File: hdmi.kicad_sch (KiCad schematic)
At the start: 43 parts, among them J13 46756-1001, Q22 NX138BKMYL, U43 NTS0102GT, U44 TPD4E02B04DQA, U45 TPD4E02B04DQA, U46 TPD4E02B04DQA

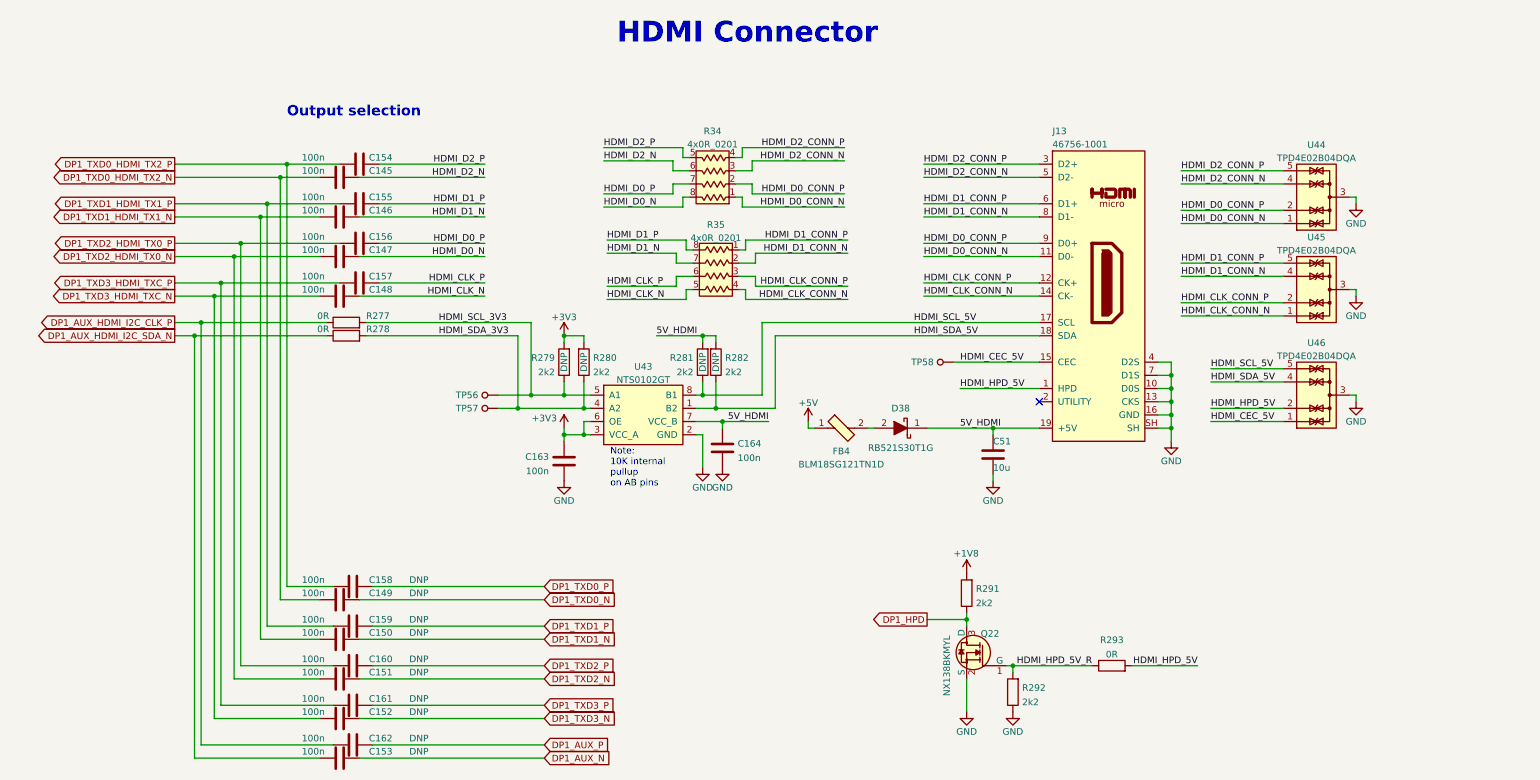
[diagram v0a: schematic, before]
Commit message: Routed high speed HDMI/DP
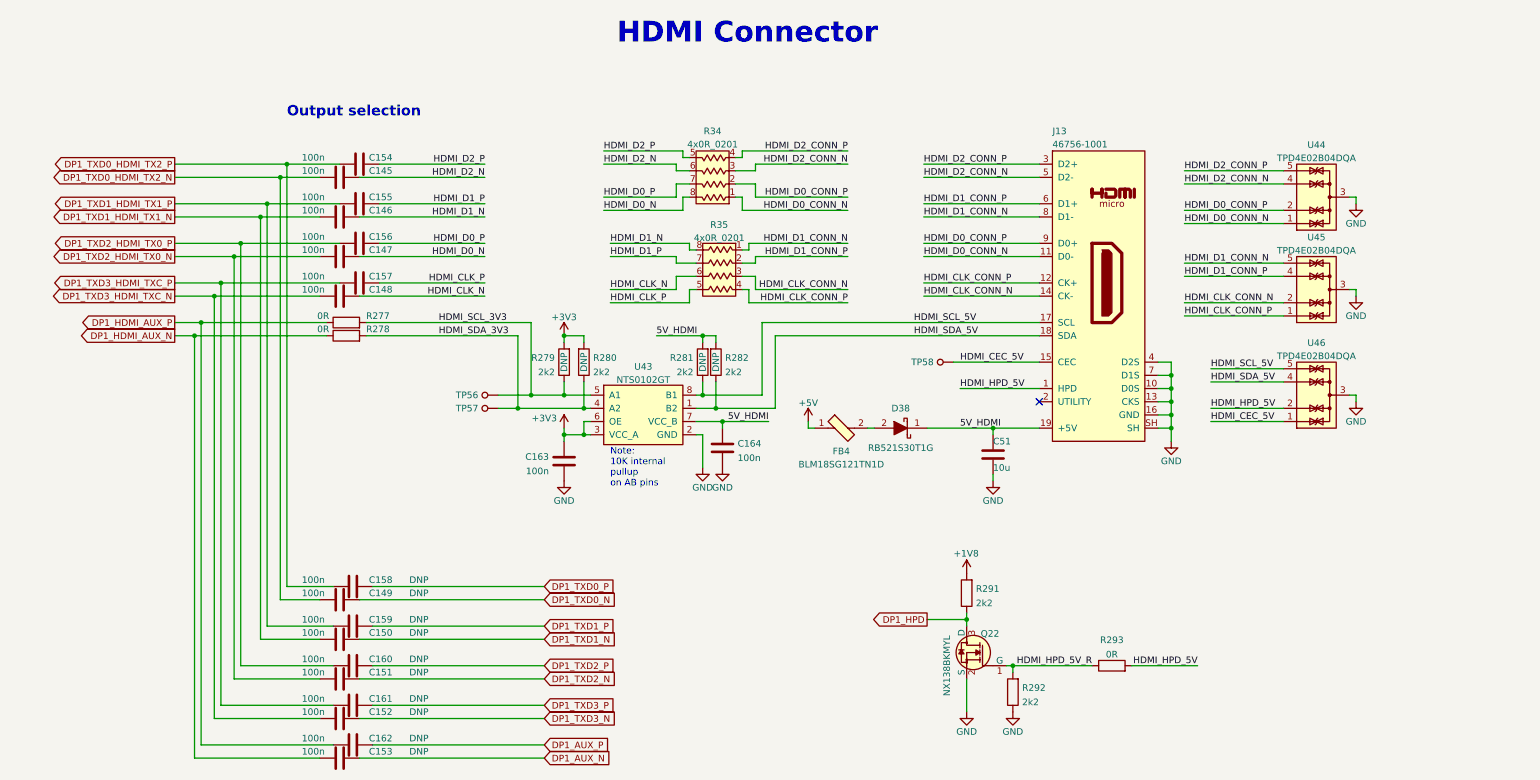
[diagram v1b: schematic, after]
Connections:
- net HDMI_CLK_CONN_N: now also R35.3, U45.2 (IO2), U45.9 (NC); no longer R35.4, U45.1 (IO1), U45.10 (NC)
- net HDMI_CLK_CONN_P: now also R35.4, U45.1 (IO1), U45.10 (NC); no longer R35.3, U45.2 (IO2), U45.9 (NC)
- net HDMI_CLK_N: now also R35.6; no longer R35.5
- net HDMI_CLK_P: now also R35.5; no longer R35.6
- net HDMI_D1_CONN_N: now also R35.1, U45.5 (IO4), U45.6 (NC); no longer R35.2, U45.4 (IO3), U45.7 (NC)
- net HDMI_D1_CONN_P: now also R35.2, U45.4 (IO3), U45.7 (NC); no longer R35.1, U45.5 (IO4), U45.6 (NC)
- net HDMI_D1_N: now also R35.8; no longer R35.7
- net HDMI_D1_P: now also R35.7; no longer R35.8
- net DP1_AUX_HDMI_I2C_CLK_P renamed DP1_HDMI_AUX_P
- net DP1_AUX_HDMI_I2C_SDA_N renamed DP1_HDMI_AUX_N
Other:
- moved on the sheet: R35

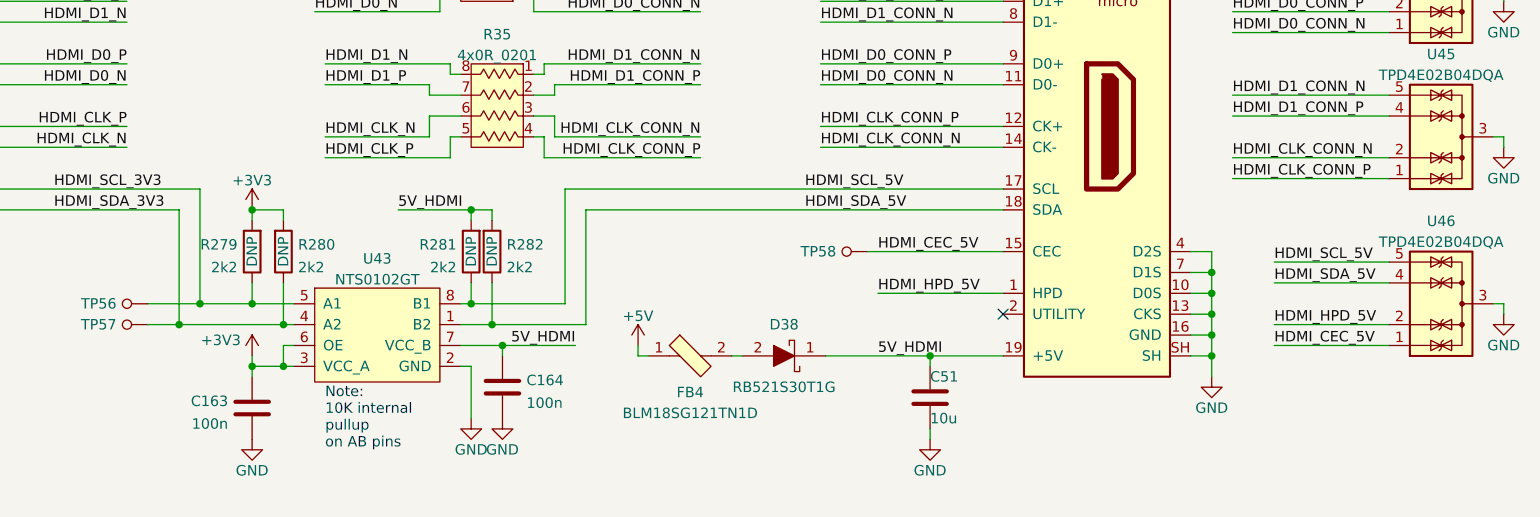
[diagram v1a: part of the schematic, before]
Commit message: Routed more low speed signal and power
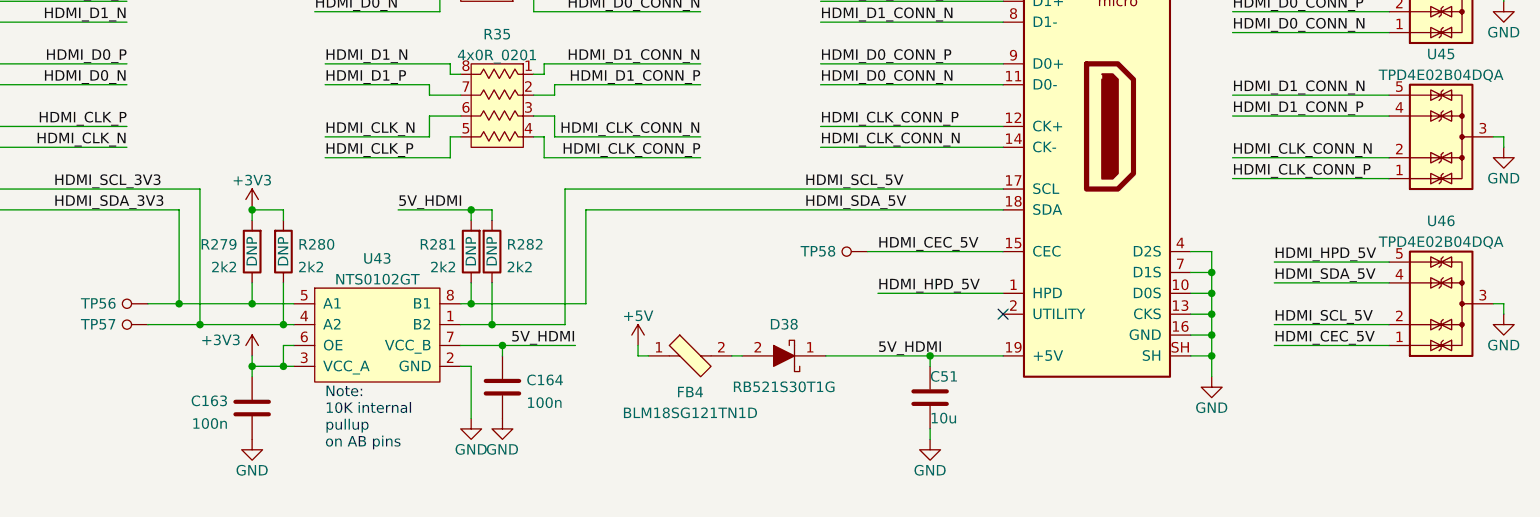
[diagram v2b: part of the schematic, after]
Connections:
- net HDMI_HPD_5V: now also U46.5 (IO4), U46.6 (NC); no longer U46.2 (IO2), U46.9 (NC)
- net HDMI_SCL_3V3: now also R280.1, TP57.1, U43.4 (A2); no longer R279.1, TP56.1, U43.5 (A1)
- net HDMI_SCL_5V: now also R282.1, U43.1 (B2), U46.2 (IO2), U46.9 (NC); no longer R281.1, U43.8 (B1), U46.5 (IO4), U46.6 (NC)
- net HDMI_SDA_3V3: now also R279.1, TP56.1, U43.5 (A1); no longer R280.1, TP57.1, U43.4 (A2)
- net HDMI_SDA_5V: now also R281.1, U43.8 (B1); no longer R282.1, U43.1 (B2)

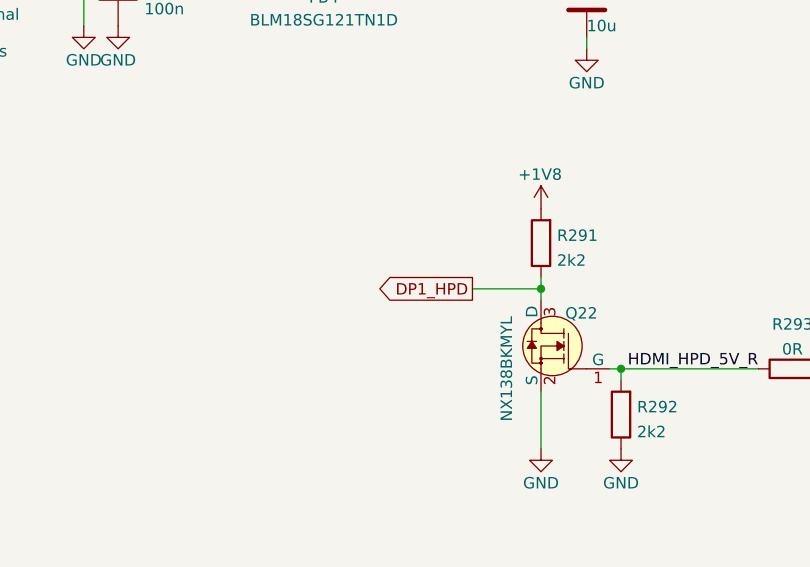
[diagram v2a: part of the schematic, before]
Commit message: CSchematic changes after review
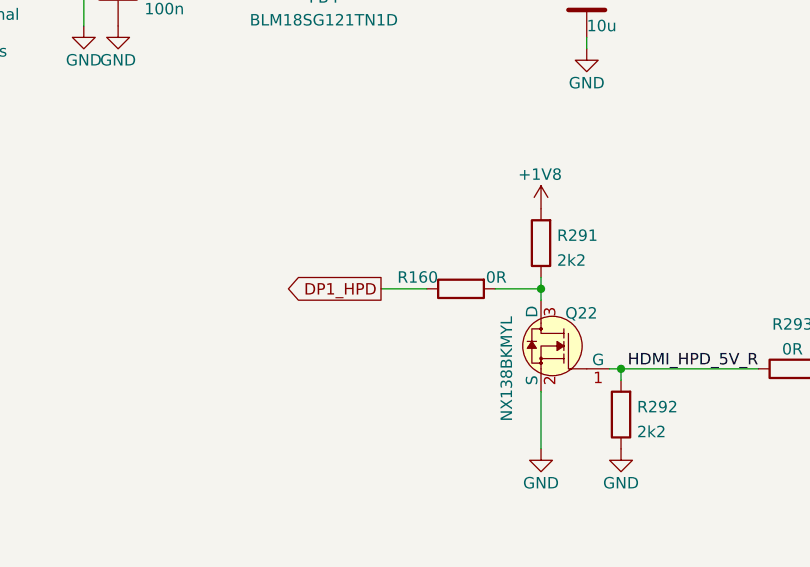
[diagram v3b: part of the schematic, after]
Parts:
- added R160: R_0R_0402, antmicro-footprints:0402-res, symbol antmicroResistors0402:R_0R_0402
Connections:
- net DP1_HPD: now also R160.1; no longer Q22.3 (D), R291.1
- new net: Q22.3 (D), R160.2, R291.1
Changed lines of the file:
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@@
   (junction (at 109.22 106.68) (diameter 0) (color 0 0 0 0)
   )
-  (junction (at 250.19 176.53) (diameter 0) (color 0 0 0 0)
-  )
   (junction (at 110.49 104.14) (diameter 0) (color 0 0 0 0)
   )
+  (junction (at 250.19 176.53) (diameter 0) (color 0 0 0 0)
+  )
   (junction (at 101.6 121.92) (diameter 0) (color 0 0 0 0)
   )
@@
     (stroke (width 0) (type default) (color 0 0 0 0))
   )
-  (wire (pts (xy 242.57 176.53) (xy 250.19 176.53))
-    (stroke (width 0) (type default) (color 0 0 0 0))
-  )
   (wire (pts (xy 247.65 127) (xy 264.16 127))
     (stroke (width 0) (type default) (color 0 0 0 0))
@@
     (stroke (width 0) (type default) (color 0 0 0 0))
   )
+  (wire (pts (xy 245.11 176.53) (xy 250.19 176.53))
+    (stroke (width 0) (type default) (color 0 0 0 0))
+  )
   (wire (pts (xy 168.91 170.18) (xy 135.89 170.18))
     (stroke (width 0) (type default) (color 0 0 0 0))
@@
     (stroke (width 0) (type default) (color 0 0 0 0))
   )
+  (wire (pts (xy 250.19 176.53) (xy 250.19 177.8))
+    (stroke (width 0) (type default) (color 0 0 0 0))
+  )
   (wire (pts (xy 166.37 135.89) (xy 176.53 135.89))
     (stroke (width 0) (type default) (color 0 0 0 0))
@@
     (stroke (width 0) (type default) (color 0 0 0 0))
   )
-  (wire (pts (xy 250.19 177.8) (xy 250.19 176.53))
+  (wire (pts (xy 250.19 175.26) (xy 250.19 176.53))
     (stroke (width 0) (type default) (color 0 0 0 0))
   )
@@
     (stroke (width 0) (type default) (color 0 0 0 0))
   )
-  (wire (pts (xy 250.19 175.26) (xy 250.19 176.53))
-    (stroke (width 0) (type default) (color 0 0 0 0))
-  )
   (wire (pts (xy 106.68 193.04) (xy 128.27 193.04))
     (stroke (width 0) (type default) (color 0 0 0 0))
@@
     (stroke (width 0) (type default) (color 0 0 0 0))
   )
+  (wire (pts (xy 232.41 176.53) (xy 237.49 176.53))
+    (stroke (width 0) (type default) (color 0 0 0 0))
+  )
   (wire (pts (xy 177.8 138.43) (xy 176.53 138.43))
     (stroke (width 0) (type default) (color 0 0 0 0))
@@
     )
   )
-  (global_label "DP1_HPD" (shape output) (at 242.57 176.53 180)
+  (global_label "DP1_HPD" (shape output) (at 232.41 176.53 180)
     (effects (font (size 1.27 1.27)) (justify right))
-    (property "Intersheet References" "${INTERSHEET_REFS}" (id 0) (at 228.6 176.53 0)
+    (property "Intersheet References" "${INTERSHEET_REFS}" (id 0) (at 218.44 176.53 0)
       (effects (font (size 1.27 1.27)) (justify right))
     )
@@
     (pin "1")
     (pin "2")
+  )
+  (symbol (lib_id "antmicroResistors0402:R_0R_0402") (at 241.3 176.53 0) (mirror x) (unit 1)
+    (in_bom yes) (on_board yes)
+    (property "Reference" "R160" (id 0) (at 238.76 175.26 0)
+      (effects (font (size 1.27 1.27)) (justify right))
+    )
+    (property "Value" "R_0R_0402" (id 1) (at 241.3 172.72 0)
+      (effects (font (size 1.27 1.27)) hide)
+    )
+    (property "Footprint" "antmicro-footprints:0402-res" (id 2) (at 246.38 181.61 0)
+      (effects (font (size 1.524 1.524)) (justify left) hide)
+    )
+    (property "Datasheet" "" (id 3) (at 241.3 176.53 0)
+      (effects (font (size 1.27 1.27)) hide)
+    )
+    (property "Manufacturer" "PANASONIC" (id 4) (at 246.38 186.69 0)
+      (effects (font (size 1.524 1.524)) (justify left) hide)
+    )
+    (property "MPN" "ERJ2GE0R00X" (id 5) (at 246.38 184.15 0)
+      (effects (font (size 1.524 1.524)) (justify left) hide)
+    )
+    (property "Val" "0R" (id 6) (at 246.38 175.26 0)
+      (effects (font (size 1.27 1.27)) (justify right))
+    )
+    (pin "1")
+    (pin "2")

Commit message: Loclib
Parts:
- C145, C146, C147, C148, C149, C150, C151, C152, C153, C154, C155, C156, C157, C158, C159, C160, C161, C162, C163, C164: footprint antmicro-footprints:0402-cap -> jetson-orin-baseboard-footprints:0402-cap; symbol antmicroCapacitors0402:C_100n_0402 -> jetson-orin-baseboard:C_100n_0402
- C51: footprint antmicro-footprints:0603-cap -> jetson-orin-baseboard-footprints:0603-cap; symbol antmicroCapacitors0603:C_10u_0603 -> jetson-orin-baseboard:C_10u_0603
- D38: footprint antmicro-footprints:SOD-523 -> jetson-orin-baseboard-footprints:SOD-523; symbol antmicroDiodesRectifiersSingle:RB521S30T1G -> jetson-orin-baseboard:RB521S30T1G
- FB4: footprint antmicro-footprints:0603-res -> jetson-orin-baseboard-footprints:0603-res; symbol antmicroFerriteBeadsandChips:BLM18SG121TN1D -> jetson-orin-baseboard:BLM18SG121TN1D
- J13: footprint antmicro-footprints:HDMI_Micro-D_Molex_46765-1x01 -> jetson-orin-baseboard-footprints:HDMI_Micro-D_Molex_46765-1x01; symbol antmicroUSBDVIHDMIConnectors:46756-1001 -> jetson-orin-baseboard:46756-1001
- Q22: footprint antmicro-footprints:DFN1006-3 -> jetson-orin-baseboard-footprints:DFN1006-3; symbol antmicroTransistorsFETsMOSFETsSingle:NX138BKMYL -> jetson-orin-baseboard:NX138BKMYL
- R160, R277, R278, R293: footprint antmicro-footprints:0402-res -> jetson-orin-baseboard-footprints:0402-res; symbol antmicroResistors0402:R_0R_0402 -> jetson-orin-baseboard:R_0R_0402
- R279, R280, R281, R282, R291, R292: footprint antmicro-footprints:0402-res -> jetson-orin-baseboard-footprints:0402-res; symbol antmicroResistors0402:R_2k2_0402 -> jetson-orin-baseboard:R_2k2_0402
- R34, R35: footprint antmicro-footprints:EXB18V -> jetson-orin-baseboard-footprints:EXB18V; symbol antmicroResistorNetworksArrays:4x0R_0201_array -> jetson-orin-baseboard:4x0R_0201_array
- TP56, TP57, TP58: footprint antmicro-footprints:Testpoint_smd_0_75mm -> jetson-orin-baseboard-footprints:Testpoint_smd_0_75mm; symbol antmicroTestPoints:TP_SMD_0_75MM -> jetson-orin-baseboard:TP_SMD_0_75MM
- U43: footprint antmicro-footprints:PSON50P100X195X50-8N -> jetson-orin-baseboard-footprints:PSON50P100X195X50-8N; symbol antmicroLogicTranslatorsLevelShifters:NTS0102GT -> jetson-orin-baseboard:NTS0102GT
- U44, U45, U46: footprint antmicro-footprints:USON-10_2.5x1.0mm_P0.5mm -> jetson-orin-baseboard-footprints:USON-10_2.5x1.0mm_P0.5mm; symbol antmicroTVSDiodes:TPD4E02B04DQA -> jetson-orin-baseboard:TPD4E02B04DQA
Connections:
- net GND: no longer U45.3 (G), U45.8 (G), U46.3 (G), U46.8 (G)
- net HDMI_CEC_5V: no longer U46.1 (IO1), U46.10 (NC)
- net HDMI_CLK_CONN_N: no longer R35.3, U45.2 (IO2), U45.9 (NC)
- net HDMI_CLK_CONN_P: no longer R35.4, U45.1 (IO1), U45.10 (NC)
- net HDMI_CLK_N: no longer R35.6
- net HDMI_CLK_P: no longer R35.5
- net HDMI_D0_CONN_N: no longer R34.1
- net HDMI_D0_CONN_P: no longer R34.2
- net HDMI_D0_N: no longer R34.8
- net HDMI_D0_P: no longer R34.7
- net HDMI_D1_CONN_N: no longer R35.1, U45.5 (IO4), U45.6 (NC)
- net HDMI_D1_CONN_P: no longer R35.2, U45.4 (IO3), U45.7 (NC)
- net HDMI_D1_N: no longer R35.8
- net HDMI_D1_P: no longer R35.7
- net HDMI_D2_CONN_N: no longer R34.3
- net HDMI_D2_CONN_P: no longer R34.4
- net HDMI_D2_N: no longer R34.6
- net HDMI_D2_P: no longer R34.5
- net HDMI_HPD_5V: no longer U46.5 (IO4), U46.6 (NC)
- net HDMI_SCL_5V: no longer U46.2 (IO2), U46.9 (NC)
- net HDMI_SDA_5V: no longer U46.4 (IO3), U46.7 (NC)

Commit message: Fix symbols after loclib
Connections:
- net GND: now also U45.3 (G), U45.8 (G), U46.3 (G), U46.8 (G)
- net HDMI_CEC_5V: now also U46.1 (IO1), U46.10 (NC)
- net HDMI_CLK_CONN_N: now also R35.3, U45.2 (IO2), U45.9 (NC)
- net HDMI_CLK_CONN_P: now also R35.4, U45.1 (IO1), U45.10 (NC)
- net HDMI_CLK_N: now also R35.6
- net HDMI_CLK_P: now also R35.5
- net HDMI_D0_CONN_N: now also R34.1
- net HDMI_D0_CONN_P: now also R34.2
- net HDMI_D0_N: now also R34.8
- net HDMI_D0_P: now also R34.7
- net HDMI_D1_CONN_N: now also R35.1, U45.5 (IO4), U45.6 (NC)
- net HDMI_D1_CONN_P: now also R35.2, U45.4 (IO3), U45.7 (NC)
- net HDMI_D1_N: now also R35.8
- net HDMI_D1_P: now also R35.7
- net HDMI_D2_CONN_N: now also R34.3
- net HDMI_D2_CONN_P: now also R34.4
- net HDMI_D2_N: now also R34.6
- net HDMI_D2_P: now also R34.5
- net HDMI_HPD_5V: now also U46.5 (IO4), U46.6 (NC)
- net HDMI_SCL_5V: now also U46.2 (IO2), U46.9 (NC)
- net HDMI_SDA_5V: now also U46.4 (IO3), U46.7 (NC)
